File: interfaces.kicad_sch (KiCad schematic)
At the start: 38 parts, among them J16 Conn_02x12_Odd_Even, J3 Conn_01x15_Female, J4 Bus_M.2_Socket_E, Q1 BSS138APW, Q2 BSS138APW

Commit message: Checkpoint
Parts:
- added SP3: 9774015151R, jetson-nano-baseboard-footprints:M2.5-2.5mm, symbol jetson-nano-baseboard:9774040151
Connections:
- net 3V3_SYS: now also J16.23 (Pin_23); no longer J16.19 (Pin_19)
- net GND: now also SP3.1
- net USB_VBUS: now also J16.19 (Pin_19), J16.21 (Pin_21); no longer J16.22 (Pin_22), J16.24 (Pin_24)
- net USB1_D_P: now reaches J16.10 (Pin_10)
- net USB1_D_N: now reaches J16.12 (Pin_12)
- net USBSS_TX_P: now reaches J16.16 (Pin_16)
- net USBSS_TX_N: now reaches J16.18 (Pin_18)
- net USBSS_RX_P: now reaches J16.4 (Pin_4)
- net USBSS_RX_N: now reaches J16.6 (Pin_6)

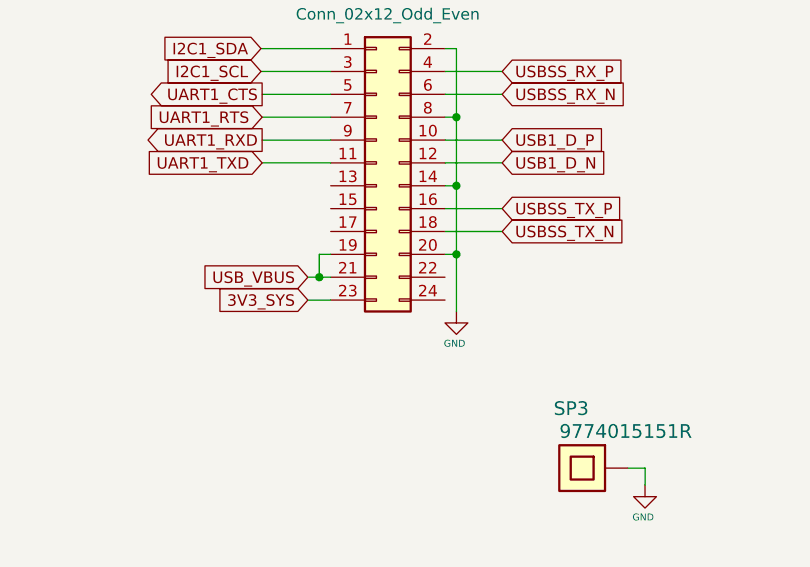
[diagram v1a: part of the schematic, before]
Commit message: Change 3v regulator. More layout
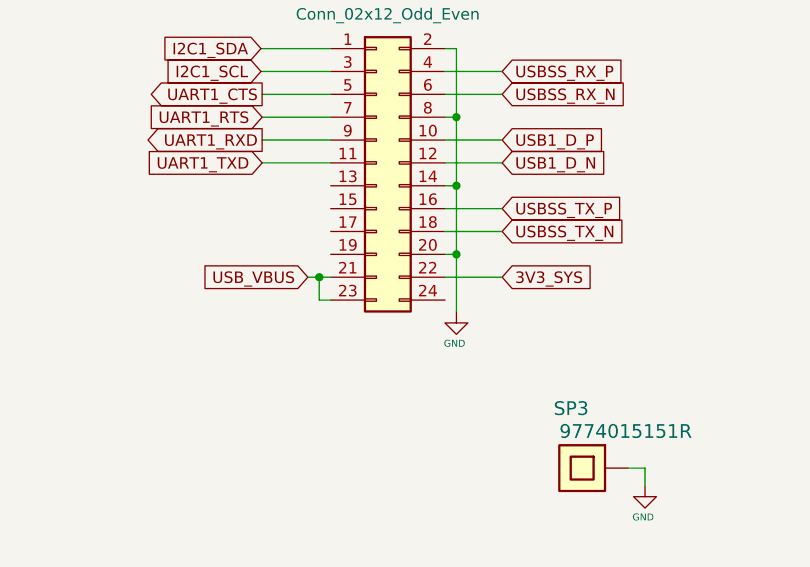
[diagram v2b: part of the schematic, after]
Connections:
- net 3V3_SYS: now also J16.22 (Pin_22); no longer J16.23 (Pin_23)
- net USB_VBUS: now also J16.23 (Pin_23); no longer J16.19 (Pin_19)

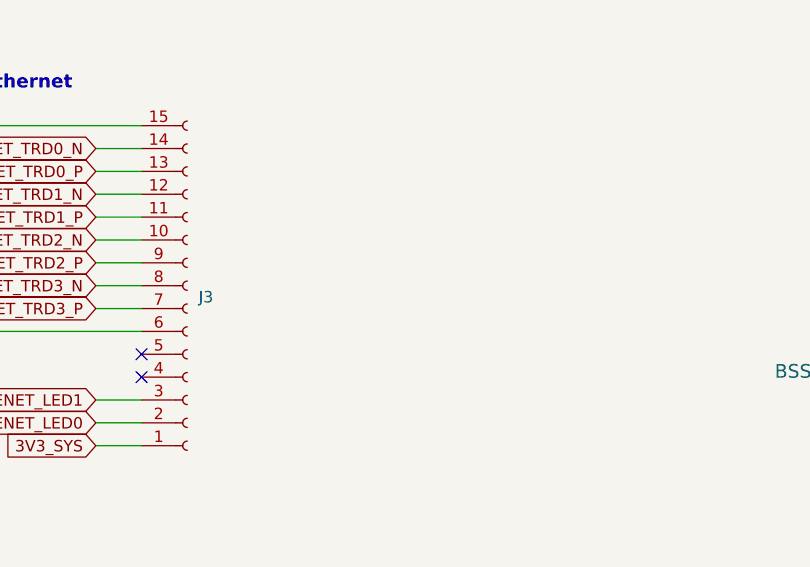
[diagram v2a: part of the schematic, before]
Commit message: Add I2S FFC
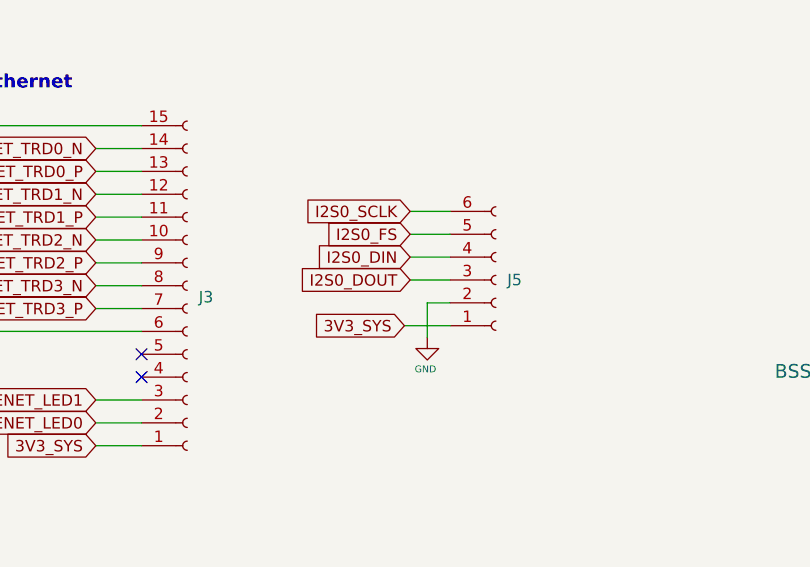
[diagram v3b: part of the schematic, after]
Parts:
- added J5: (no value), symbol Connector:Conn_01x06_Female
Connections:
- net 3V3_SYS: now also J5.1 (Pin_1)
- net GND: now also J5.2 (Pin_2)
- new net I2S0_DIN: J5.4 (Pin_4)
- new net I2S0_DOUT: J5.3 (Pin_3)
- new net I2S0_FS: J5.5 (Pin_5)
- new net I2S0_SCLK: J5.6 (Pin_6)
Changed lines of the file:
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@@
+    (stroke (width 0) (type default) (color 0 0 0 0))
+  )
+  (wire (pts (xy 261.62 50.165) (xy 259.08 50.165))
     (stroke (width 0) (type default) (color 0 0 0 0))
   )
@@
     (stroke (width 0) (type default) (color 0 0 0 0))
   )
+  (wire (pts (xy 257.175 42.545) (xy 261.62 42.545))
+    (stroke (width 0) (type default) (color 0 0 0 0))
+  )
   (wire (pts (xy 285.75 160.02) (xy 291.465 160.02))
     (stroke (width 0) (type default) (color 0 0 0 0))
@@
     (stroke (width 0) (type default) (color 0 0 0 0))
   )
+  (wire (pts (xy 259.08 50.165) (xy 259.08 53.975))
+    (stroke (width 0) (type default) (color 0 0 0 0))
+  )
   (wire (pts (xy 90.805 203.2) (xy 90.805 200.66))
     (stroke (width 0) (type default) (color 0 0 0 0))
@@
     (stroke (width 0) (type default) (color 0 0 0 0))
   )
+  (wire (pts (xy 256.54 52.705) (xy 261.62 52.705))
+    (stroke (width 0) (type default) (color 0 0 0 0))
+  )
   (wire (pts (xy 80.645 120.65) (xy 80.645 131.445))
     (stroke (width 0) (type default) (color 0 0 0 0))
@@
     (stroke (width 0) (type default) (color 0 0 0 0))
   )
+  (wire (pts (xy 257.175 45.085) (xy 261.62 45.085))
+    (stroke (width 0) (type default) (color 0 0 0 0))
+  )
   (wire (pts (xy 368.3 48.895) (xy 393.7 48.895))
     (stroke (width 0) (type default) (color 0 0 0 0))
@@
     (stroke (width 0) (type default) (color 0 0 0 0))
   )
+  (wire (pts (xy 257.175 47.625) (xy 261.62 47.625))
+    (stroke (width 0) (type default) (color 0 0 0 0))
+  )
   (wire (pts (xy 113.665 193.04) (xy 113.665 195.58))
     (stroke (width 0) (type default) (color 0 0 0 0))
@@
   )
   (wire (pts (xy 129.54 48.26) (xy 135.89 48.26))
+    (stroke (width 0) (type default) (color 0 0 0 0))
+  )
+  (wire (pts (xy 257.175 40.005) (xy 261.62 40.005))
     (stroke (width 0) (type default) (color 0 0 0 0))
   )
@@
     )
   )
+  (global_label "I2S0_FS" (shape input) (at 257.175 42.545 180) (fields_autoplaced)
+    (effects (font (size 1.27 1.27)) (justify right))
+    (property "Intersheet References" "${INTERSHEET_REFS}" (id 0) (at 247.3518 42.4656 0)
+      (effects (font (size 1.27 1.27)) (justify right) hide)
+    )
+  )
   (global_label "I2C1_SDA" (shape input) (at 109.093 38.1 180) (fields_autoplaced)
     (effects (font (size 1.27 1.27)) (justify right))
@@
     )
   )
+  (global_label "I2S0_SCLK" (shape input) (at 257.175 40.005 180) (fields_autoplaced)
+    (effects (font (size 1.27 1.27)) (justify right))
+    (property "Intersheet References" "${INTERSHEET_REFS}" (id 0) (at 244.8722 39.9256 0)
+      (effects (font (size 1.27 1.27)) (justify right) hide)
+    )
+  )
   (global_label "3V3_SYS" (shape input) (at 368.3 36.195 90) (fields_autoplaced)
     (effects (font (size 1.27 1.27)) (justify left))
@@
     )
   )
+  (global_label "I2S0_DOUT" (shape input) (at 257.175 47.625 180) (fields_autoplaced)
+    (effects (font (size 1.27 1.27)) (justify right))
+    (property "Intersheet References" "${INTERSHEET_REFS}" (id 0) (at 244.7513 47.5456 0)
+      (effects (font (size 1.27 1.27)) (justify right) hide)
+    )
+  )
   (global_label "ENET_TRD0_P" (shape input) (at 222.25 35.56 180) (fields_autoplaced)
     (effects (font (size 1.27 1.27)) (justify right))
@@
     )
   )
+  (global_label "I2S0_DIN" (shape input) (at 257.175 45.085 180) (fields_autoplaced)
+    (effects (font (size 1.27 1.27)) (justify right))
+    (property "Intersheet References" "${INTERSHEET_REFS}" (id 0) (at 246.4446 45.0056 0)
+      (effects (font (size 1.27 1.27)) (justify right) hide)
+    )
+  )
   (global_label "PCIE1_CLKREQ" (shape input) (at 298.45 129.54 180) (fields_autoplaced)
     (effects (font (size 1.27 1.27)) (justify right))
@@
     (property "Intersheet References" "${INTERSHEET_REFS}" (id 0) (at 378.3652 180.2606 0)
       (effects (font (size 1.27 1.27)) (justify left) hide)
+    )
+  )
+  (global_label "3V3_SYS" (shape input) (at 256.54 52.705 180) (fields_autoplaced)
+    (effects (font (size 1.27 1.27)) (justify right))
+    (property "Intersheet References" "${INTERSHEET_REFS}" (id 0) (at -28.575 -81.915 0)
+      (effects (font (size 1.27 1.27)) hide)
     )
   )
@@
     (pin "9")
   )
+  (symbol (lib_id "Connector:Conn_01x06_Female") (at 266.7 47.625 0) (mirror x) (unit 1)
+    (in_bom yes) (on_board yes) (fields_autoplaced)
+    (property "Reference" "J5" (id 0) (at 267.97 47.6251 0)
+      (effects (font (size 1.27 1.27)) (justify left))
+    )
+    (property "Value" "" (id 1) (at 267.97 45.0851 0)
+      (effects (font (size 1.27 1.27)) (justify left) hide)
+    )
+    (property "Footprint" "" (id 2) (at 266.7 47.625 0)
+      (effects (font (size 1.27 1.27)) hide)
+    )
+    (property "Datasheet" "~" (id 3) (at 266.7 47.625 0)
+      (effects (font (size 1.27 1.27)) hide)
+    )
+    (pin "1")
+    (pin "2")
+    (pin "3")
+    (pin "4")
+    (pin "5")
+    (pin "6")
+  )
   (symbol (lib_id "jetson-nano-baseboard:R_220R_0402") (at 365.76 144.78 0) (unit 1)
     (in_bom yes) (on_board yes)
@@
     (pin "2")
   )
+  (symbol (lib_id "jetson-nano-baseboard:GND") (at 259.08 53.975 0) (unit 1)
+    (in_bom yes) (on_board yes)
+    (property "Reference" "#GND_039" (id 0) (at 259.08 53.975 0)
+      (effects (font (size 0.508 0.508)) hide)
+    )
+    (property "Value" "GND" (id 1) (at 258.8768 57.531 0)
+      (effects (font (size 0.762 0.762)))
+    )
+    (property "Footprint" "" (id 2) (at 259.08 53.975 0)
+      (effects (font (size 1.778 1.778)) hide)
+    )
+    (property "Datasheet" "" (id 3) (at 259.08 53.975 0)
+      (effects (font (size 1.778 1.778)) hide)
+    )
+    (pin "1")
+  )
   (symbol (lib_id "jetson-nano-baseboard:R_220R_0402") (at 97.155 162.56 0) (unit 1)

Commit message: Checkpoint
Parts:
- J5: value (none) -> Conn_01x06_Female; footprint (none) -> Connector_FFC-FPC:Hirose_FH12-6S-0.5SH_1x06-1MP_P0.50mm_Horizontal
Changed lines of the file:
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@@
       (effects (font (size 1.27 1.27)) (justify left))
     )
-    (property "Value" "" (id 1) (at 267.97 45.0851 0)
+    (property "Value" "Conn_01x06_Female" (id 1) (at 267.97 45.0851 0)
       (effects (font (size 1.27 1.27)) (justify left) hide)
     )
-    (property "Footprint" "" (id 2) (at 266.7 47.625 0)
+    (property "Footprint" "Connector_FFC-FPC:Hirose_FH12-6S-0.5SH_1x06-1MP_P0.50mm_Horizontal" (id 2) (at 266.7 47.625 0)
       (effects (font (size 1.27 1.27)) hide)
     )

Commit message: Checkpoint
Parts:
- removed J16: Conn_02x12_Odd_Even, capablerobot-footprints:DF40C-24DP-0.4V51, symbol Connector_Generic:Conn_02x12_Odd_Even
- removed NVME1: ~, jetson-nano-baseboard-footprints:LED0603, symbol jetson-nano-baseboard:LED
- added C30: C_10u_0603, Capacitor_SMD:C_0603_1608Metric, symbol jetson-nano-baseboard:C_10u_0603
- added C33: C_100n_0402, Capacitor_SMD:C_0402_1005Metric, symbol jetson-nano-baseboard:C_100n_0402
- added J13: Conn_02x10_Odd_Even, capablerobot-footprints:DF40C-20DP-0.4V51, symbol Connector_Generic:Conn_02x10_Odd_Even
- added NVME1: LED, LED_SMD:LED_0603_1608Metric, symbol Device:LED
- added R133: R_10k_0402, jetson-nano-baseboard-footprints:0402-res, symbol jetson-nano-baseboard:R_10k_0402
- C46: footprint jetson-nano-baseboard-footprints:0402-cap -> Capacitor_SMD:C_0402_1005Metric
- C47: footprint jetson-nano-baseboard-footprints:0603-cap -> Capacitor_SMD:C_0603_1608Metric
- R4: MPN CRCW040210K0FKEDHP -> (none); Manufacturer VISHAY -> (none); Val 10k -> DNP
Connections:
- net 1V8_SYS: now also R133.1
- net 3V3_SYS: now also C30.2, C33.2, J13.17 (Pin_17), J13.19 (Pin_19)
- net BT_M2_WAKE_AP: now also R133.2
- net GND: now also C30.1, C33.1, J13.14 (Pin_14), J13.2 (Pin_2), J13.20 (Pin_20), J13.8 (Pin_8)
- net I2C1_SCL: now also J13.3 (Pin_3)
- net I2C1_SDA: now also J13.1 (Pin_1)
- net NVME_LED: now also NVME1.1 (K)
- net USB1_D_N: now also J13.12 (Pin_12)
- net USB1_D_P: now also J13.10 (Pin_10)
- net USBSS_RX_N: now also J13.6 (Pin_6)
- net USBSS_RX_P: now also J13.4 (Pin_4)
- net USBSS_TX_N: now also J13.18 (Pin_18)
- net USBSS_TX_P: now also J13.16 (Pin_16)
- net USB_VBUS: now also J13.11 (Pin_11), J13.13 (Pin_13), J13.7 (Pin_7), J13.9 (Pin_9)
- net at R128.1: now also NVME1.2 (A)
- net C_PCIE1_TX0_N: now reaches C2.2, J4.37 (PETn0)
- net C_PCIE1_TX0_P: now reaches C1.2, J4.35 (PETp0)
- new net GPIO07: J13.15 (Pin_15)
- new net GPIO09: J13.5 (Pin_5)
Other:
- note added: "REF design has PU to 3v3, but GPIO is 1v8"
- moved on the sheet: C1, C2, R4

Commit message: Checkpoint before v120 changes
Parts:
- R128: value R_220R_0402 -> R_470R_0402; MPN ERJ2GEJ221X -> (none); Manufacturer Panasonic -> (none); Val 220R -> 470R
- R4: value R_10k_0402 -> DNP
- R6, R7, R8, R9: value R_220R_0402 -> DNP; MPN ERJ2GEJ221X -> (none); Manufacturer Panasonic -> (none); Val 220R -> DNP
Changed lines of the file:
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@@
       (effects (font (size 1.524 1.524)) (justify left))
     )
-    (property "Value" "R_220R_0402" (id 1) (at 94.615 187.96 0)
+    (property "Value" "R_470R_0402" (id 1) (at 94.615 187.96 0)
       (effects (font (size 1.524 1.524)) hide)
     )
@@
       (effects (font (size 1.27 1.27)) hide)
     )
-    (property "Manufacturer" "Panasonic" (id 4) (at 80.645 182.88 0)
-      (effects (font (size 1.524 1.524)) (justify left) hide)
-    )
-    (property "MPN" "ERJ2GEJ221X" (id 5) (at 83.185 182.88 0)
-      (effects (font (size 1.524 1.524)) (justify left) hide)
-    )
-    (property "Val" "220R" (id 6) (at 97.155 189.23 90)
+    (property "Val" "470R" (id 6) (at 97.155 189.23 90)
       (effects (font (size 1.27 1.27)) (justify left))
     )
@@
       (effects (font (size 1.524 1.524)))
     )
-    (property "Value" "R_220R_0402" (id 1) (at 365.76 148.59 0)
+    (property "Value" "DNP" (id 1) (at 365.76 148.59 0)
       (effects (font (size 1.524 1.524)) hide)
     )
@@
       (effects (font (size 1.27 1.27)) hide)
     )
-    (property "Manufacturer" "Panasonic" (id 4) (at 370.84 134.62 0)
-      (effects (font (size 1.524 1.524)) (justify left) hide)
-    )
-    (property "MPN" "ERJ2GEJ221X" (id 5) (at 370.84 137.16 0)
-      (effects (font (size 1.524 1.524)) (justify left) hide)
-    )
-    (property "Val" "220R" (id 6) (at 365.76 144.78 0))
+    (property "Val" "DNP" (id 6) (at 365.76 144.78 0))
     (pin "1")
     (pin "2")
@@
       (effects (font (size 1.524 1.524)))
     )
-    (property "Value" "R_220R_0402" (id 1) (at 97.155 166.37 0)
+    (property "Value" "DNP" (id 1) (at 97.155 166.37 0)
       (effects (font (size 1.524 1.524)) hide)
     )
@@
       (effects (font (size 1.27 1.27)) hide)
     )
-    (property "Manufacturer" "Panasonic" (id 4) (at 102.235 152.4 0)
-      (effects (font (size 1.524 1.524)) (justify left) hide)
-    )
-    (property "MPN" "ERJ2GEJ221X" (id 5) (at 102.235 154.94 0)
-      (effects (font (size 1.524 1.524)) (justify left) hide)
-    )
-    (property "Val" "220R" (id 6) (at 97.155 162.56 0))
+    (property "Val" "DNP" (id 6) (at 97.155 162.56 0))
     (pin "1")
     (pin "2")
@@
       (effects (font (size 1.524 1.524)))
     )
-    (property "Value" "R_220R_0402" (id 1) (at 97.155 168.91 0)
+    (property "Value" "DNP" (id 1) (at 97.155 168.91 0)
       (effects (font (size 1.524 1.524)) hide)
     )
@@
       (effects (font (size 1.27 1.27)) hide)
     )
-    (property "Manufacturer" "Panasonic" (id 4) (at 102.235 154.94 0)
-      (effects (font (size 1.524 1.524)) (justify left) hide)
-    )
-    (property "MPN" "ERJ2GEJ221X" (id 5) (at 102.235 157.48 0)
-      (effects (font (size 1.524 1.524)) (justify left) hide)
-    )
-    (property "Val" "220R" (id 6) (at 97.155 165.1 0))
+    (property "Val" "DNP" (id 6) (at 97.155 165.1 0))
     (pin "1")
     (pin "2")
@@
       (effects (font (size 1.524 1.524)) (justify left))
     )
-    (property "Value" "R_10k_0402" (id 1) (at 384.175 166.37 0)
+    (property "Value" "DNP" (id 1) (at 384.175 166.37 0)
       (effects (font (size 1.524 1.524)) hide)
     )
@@
       (effects (font (size 1.524 1.524)))
     )
-    (property "Value" "R_220R_0402" (id 1) (at 365.76 146.05 0)
+    (property "Value" "DNP" (id 1) (at 365.76 146.05 0)
       (effects (font (size 1.524 1.524)) hide)
     )
@@
       (effects (font (size 1.27 1.27)) hide)
     )
-    (property "Manufacturer" "Panasonic" (id 4) (at 370.84 132.08 0)
-      (effects (font (size 1.524 1.524)) (justify left) hide)
-    )
-    (property "MPN" "ERJ2GEJ221X" (id 5) (at 370.84 134.62 0)
-      (effects (font (size 1.524 1.524)) (justify left) hide)
-    )
-    (property "Val" "220R" (id 6) (at 365.76 142.24 0))
-    (pin "1")
-    (pin "2")
+    (property "Val" "DNP" (id 6) (at 365.76 142.24 0))
+    (pin "1")
+    (pin "2")

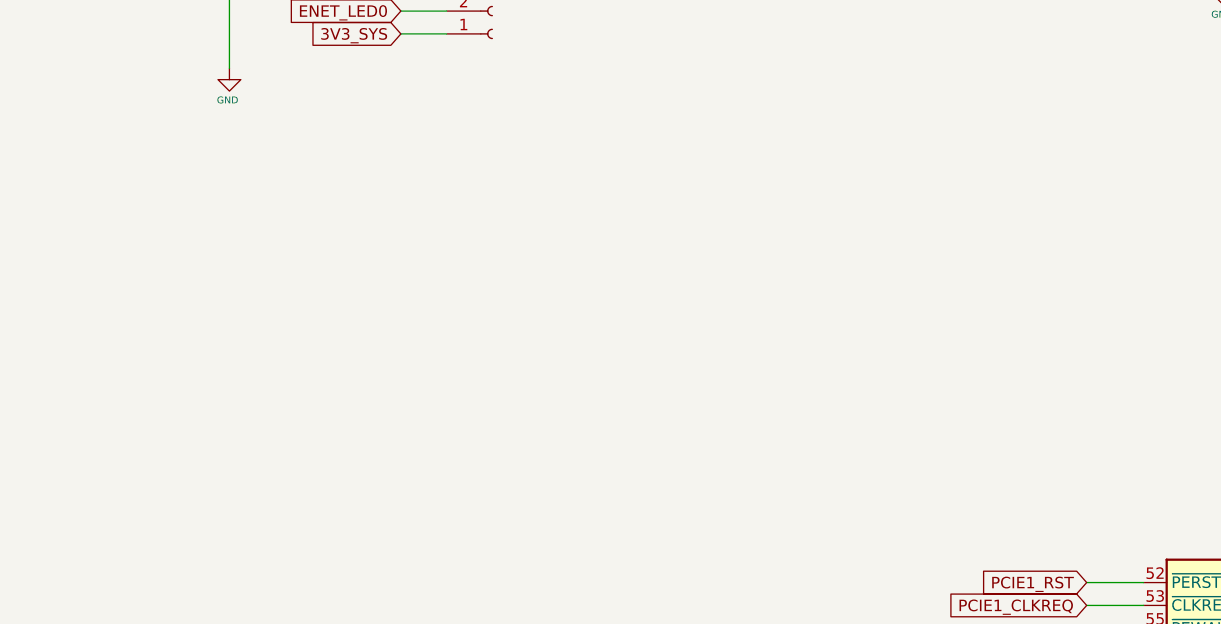
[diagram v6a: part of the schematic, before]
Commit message: Add CAN transceiver.  Clean up DRC warnings
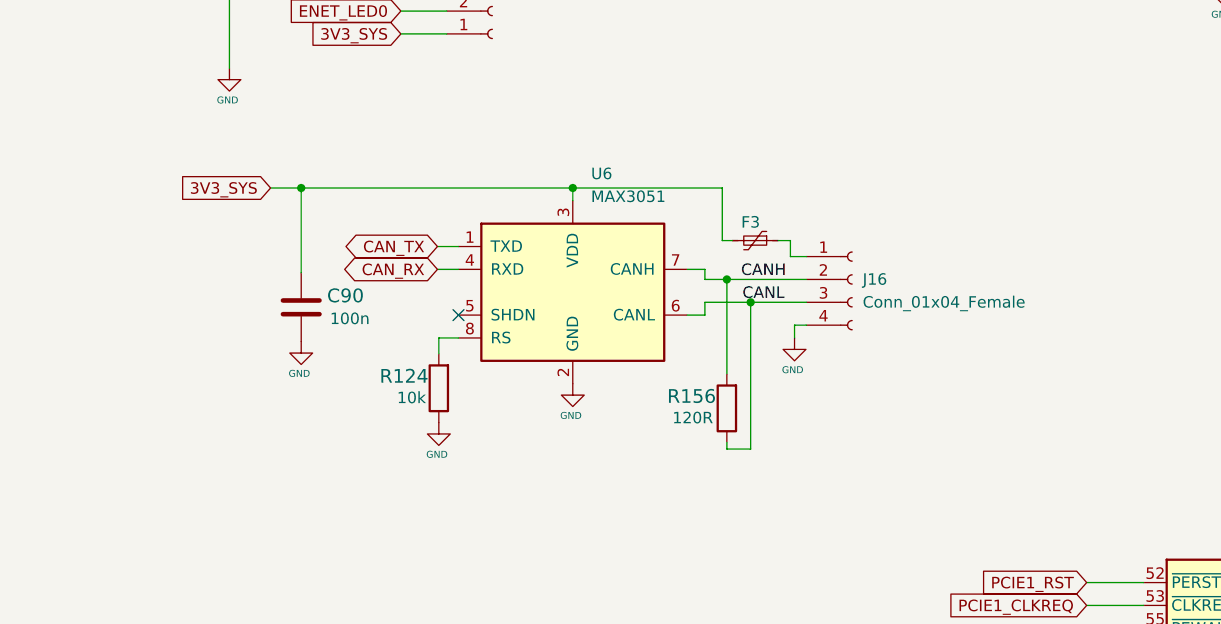
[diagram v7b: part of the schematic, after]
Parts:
- added C90: C_100n_0402, Capacitor_SMD:C_0402_1005Metric, symbol jetson-nano-baseboard:C_100n_0402
- added F3: Polyfuse_Small, Fuse:Fuse_0603_1608Metric, symbol Device:Polyfuse_Small
- added J16: Conn_01x04_Female, Connector_Molex:Molex_Pico-Lock_504050-0491_1x04-1MP_P1.50mm_Horizontal, symbol Connector:Conn_01x04_Female
- added R124: R_10k_0402, jetson-nano-baseboard-footprints:0402-res, symbol jetson-nano-baseboard:R_10k_0402
- added R156: R_120R_0603, Resistor_SMD:R_0603_1608Metric, symbol jetson-nano-baseboard:R_10k_0402
- added U6: MAX3051, Package_TO_SOT_SMD:SOT-23-8, symbol Interface_UART:MAX3051
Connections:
- net 3V3_SYS: now also C90.2, F3.2, U6.3 (VDD)
- net GND: now also C90.1, J16.4 (Pin_4), R124.1, U6.2 (GND)
- new net: F3.1, J16.1 (Pin_1)
- new net: R124.2, U6.8 (RS)
- new net CANH: J16.2 (Pin_2), R156.2, U6.7 (CANH)
- new net CANL: J16.3 (Pin_3), R156.1, U6.6 (CANL)
- new net CAN_RX: U6.4 (RXD)
- new net CAN_TX: U6.1 (TXD)
- no-connect marks 39 -> 40
